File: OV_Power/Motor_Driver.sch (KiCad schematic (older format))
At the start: 20 parts, among them CN1 CONN_HEADER_R_A_2POS_2.5MM, U3 LT6106, U4 VNH5019ATR-E

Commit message: Changing connectors again, also fixed a library fubar...
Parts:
- removed CN1: CONN_HEADER_R_A_2POS_2.5MM, OpenVent:53426-0210, symbol OV_Power-rescue:CONN_HEADER_R_A_2POS_2.5MM-OpenVent
- added J8: CONN_HEADER_R_A_2POS_JST_10A, OpenVent:JST_B2PS-VHLSN, symbol OpenVent:CONN_HEADER_R_A_2POS_JST_10A
- C11, C12, C16, C17, C18, C19: symbol OV_Power-rescue:1000uF_25V_Aluminium_SMD_Capacitor,_20%-OpenVent -> OpenVent:1000uF_25V_Aluminium_SMD_Capacitor,_20%
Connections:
- net at R31.1, U4.1 (OUTA), U4.25 (OUTA)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: now also J8.2
- net at D5.2 (CATHODE), D6.1 (ANODE), U4.15 (OUTB)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: now also J8.1
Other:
- note removed: "Mates with Molex cable assembly 151370201"
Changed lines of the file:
@@
 	1    0    0    -1
 $EndComp
-Text Notes 8750 4500 0    60   ~ 0
-Mates with Molex cable assembly 151370201
 NoConn ~ 4550 3750
 Text GLabel 2050 3050 0    60   Output ~ 0
@@
 Wire Wire Line
 	8500 4500 7200 4500
-Wire Wire Line
-	8500 3950 8500 4500
 Wire Wire Line
 	6400 4150 6400 4050
@@
 	1    2600 3250
 	1    0    0    -1
-$EndComp
-$Comp
-L OV_Power-rescue:CONN_HEADER_R_A_2POS_2.5MM-OpenVent CN1
-U 1 1 5F8DD118
-P 8500 3850
-F 0 "CN1" H 8700 3650 50  0000 L BNN
-F 1 "CONN_HEADER_R_A_2POS_2.5MM" H 8500 3850 50  0001 C CNN
-F 2 "OpenVent:53426-0210" H 8500 3850 50  0001 C CNN
-F 3 "https://www.molex.com/pdm_docs/sd/534260210_sd.pdf" H 8500 3850 50  0001 C CNN
-F 4 "Molex" H 8500 3850 50  0001 C CNN "Mfr"
-F 5 "0534260210" H 8800 4150 50  0000 C CNN "Mfr_PN"
-	1    8500 3850
-	1    0    0    1
 $EndComp
 $Comp
@@
 $EndComp
 $Comp
-L OV_Power-rescue:1000uF_25V_Aluminium_SMD_Capacitor,_20%-OpenVent C11
+L OpenVent:1000uF_25V_Aluminium_SMD_Capacitor,_20% C11
 U 1 1 5F8DD0EF
 P 6550 1250
+AR Path="/5F8DD0EF" Ref="C11"  Part="1"
+AR Path="/5FADD2CF/5F8DD0EF" Ref="C11"  Part="1"
 F 0 "C11" V 6650 1350 50  0000 L BNN
 F 1 "1000uF_25V_Aluminium_SMD_Capacitor,_20%" V 6800 1340 50  0001 C CNN
@@
 	6400 3350 6750 3350
 $Comp
-L OV_Power-rescue:1000uF_25V_Aluminium_SMD_Capacitor,_20%-OpenVent C12
+L OpenVent:1000uF_25V_Aluminium_SMD_Capacitor,_20% C12
 U 1 1 5F9BE2A3
 P 7100 1250
+AR Path="/5F9BE2A3" Ref="C12"  Part="1"
+AR Path="/5FADD2CF/5F9BE2A3" Ref="C12"  Part="1"
 F 0 "C12" V 7159 1360 50  0000 L CNN
 F 1 "1000uF_25V_Aluminium_SMD_Capacitor,_20%" H 7100 1250 50  0001 C CNN
@@
 Wire Wire Line
 	6400 3350 6400 3550
-Wire Wire Line
-	8500 3350 8500 3850
 Wire Wire Line
 	6750 3400 6750 3350
@@
 	4200 2500 4200 3650
 $Comp
-L OV_Power-rescue:1000uF_25V_Aluminium_SMD_Capacitor,_20%-OpenVent C16
+L OpenVent:1000uF_25V_Aluminium_SMD_Capacitor,_20% C16
 U 1 1 5FE5727D
 P 7650 1250
+AR Path="/5FE5727D" Ref="C16"  Part="1"
+AR Path="/5FADD2CF/5FE5727D" Ref="C16"  Part="1"
 F 0 "C16" V 7709 1360 50  0000 L CNN
 F 1 "1000uF_25V_Aluminium_SMD_Capacitor,_20%" H 7650 1250 50  0001 C CNN
@@
 $EndComp
 $Comp
-L OV_Power-rescue:1000uF_25V_Aluminium_SMD_Capacitor,_20%-OpenVent C17
+L OpenVent:1000uF_25V_Aluminium_SMD_Capacitor,_20% C17
 U 1 1 5FE579F4
 P 8200 1250
+AR Path="/5FE579F4" Ref="C17"  Part="1"
+AR Path="/5FADD2CF/5FE579F4" Ref="C17"  Part="1"
 F 0 "C17" V 8259 1360 50  0000 L CNN
 F 1 "1000uF_25V_Aluminium_SMD_Capacitor,_20%" H 8200 1250 50  0001 C CNN
@@
 $EndComp
 $Comp
-L OV_Power-rescue:1000uF_25V_Aluminium_SMD_Capacitor,_20%-OpenVent C18
+L OpenVent:1000uF_25V_Aluminium_SMD_Capacitor,_20% C18
 U 1 1 5FE58241
 P 8750 1250
+AR Path="/5FE58241" Ref="C18"  Part="1"
+AR Path="/5FADD2CF/5FE58241" Ref="C18"  Part="1"
 F 0 "C18" V 8809 1360 50  0000 L CNN
 F 1 "1000uF_25V_Aluminium_SMD_Capacitor,_20%" H 8750 1250 50  0001 C CNN
@@
 $EndComp
 $Comp
-L OV_Power-rescue:1000uF_25V_Aluminium_SMD_Capacitor,_20%-OpenVent C19
+L OpenVent:1000uF_25V_Aluminium_SMD_Capacitor,_20% C19
 U 1 1 5FE58A16
 P 9300 1250
+AR Path="/5FE58A16" Ref="C19"  Part="1"
+AR Path="/5FADD2CF/5FE58A16" Ref="C19"  Part="1"
 F 0 "C19" V 9359 1360 50  0000 L CNN
 F 1 "1000uF_25V_Aluminium_SMD_Capacitor,_20%" H 9300 1250 50  0001 C CNN
@@
 Wire Wire Line
 	6100 2500 6100 3050
+$Comp
+L OpenVent:CONN_HEADER_R_A_2POS_JST_10A J8
+U 1 1 5FF9F011
+P 8600 3850
+F 0 "J8" H 8900 3650 50  0000 C CNN
+F 1 "CONN_HEADER_R_A_2POS_JST_10A" H 8800 4050 50  0001 C CNN
+F 2 "OpenVent:JST_B2PS-VHLSN" H 8800 4050 50  0001 C CNN
+F 3 "http://www.jst-mfg.com/product/pdf/eng/eVH.pdf" H 8800 4050 50  0001 C CNN
+F 4 "JST Sales America Inc." H 8600 3850 50  0001 C CNN "Mfr"
+F 5 "B2PS-VH(LF)(SN)" H 9100 4150 50  0000 C CNN "Mfr_PN"
+F 6 "CONN HEADER R/A 2POS 3.96MM" H 8600 3850 50  0001 C CNN "Desc"
+F 7 "Connector Header Through Hole, Right Angle 2 position 0.156\" (3.96mm)" H 8600 3850 50  0001 C CNN "Detailed"
+	1    8600 3850
+	1    0    0    1
+$EndComp
+Wire Wire Line
+	8500 3350 8500 3850
+Wire Wire Line
+	8500 3850 8600 3850
+Wire Wire Line
+	8600 3950 8500 3950
+Wire Wire Line
+	8500 3950 8500 4500
 $EndSCHEMATC

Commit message: updated notes
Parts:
- C11, C12, C16, C17, C18, C19: symbol OpenVent:1000uF_25V_Aluminium_SMD_Capacitor,_20% -> OV_Power-rescue:1000uF_25V_Aluminium_SMD_Capacitor,_20%-OpenVent
- J8: symbol OpenVent:CONN_HEADER_R_A_2POS_JST_10A -> OV_Power-rescue:CONN_HEADER_R_A_2POS_JST_10A-OpenVent
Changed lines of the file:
@@
 $EndComp
 $Comp
-L OpenVent:1000uF_25V_Aluminium_SMD_Capacitor,_20% C11
+L OV_Power-rescue:1000uF_25V_Aluminium_SMD_Capacitor,_20%-OpenVent C11
 U 1 1 5F8DD0EF
 P 6550 1250
@@
 	6400 3350 6750 3350
 $Comp
-L OpenVent:1000uF_25V_Aluminium_SMD_Capacitor,_20% C12
+L OV_Power-rescue:1000uF_25V_Aluminium_SMD_Capacitor,_20%-OpenVent C12
 U 1 1 5F9BE2A3
 P 7100 1250
@@
 	4200 2500 4200 3650
 $Comp
-L OpenVent:1000uF_25V_Aluminium_SMD_Capacitor,_20% C16
+L OV_Power-rescue:1000uF_25V_Aluminium_SMD_Capacitor,_20%-OpenVent C16
 U 1 1 5FE5727D
 P 7650 1250
@@
 $EndComp
 $Comp
-L OpenVent:1000uF_25V_Aluminium_SMD_Capacitor,_20% C17
+L OV_Power-rescue:1000uF_25V_Aluminium_SMD_Capacitor,_20%-OpenVent C17
 U 1 1 5FE579F4
 P 8200 1250
@@
 $EndComp
 $Comp
-L OpenVent:1000uF_25V_Aluminium_SMD_Capacitor,_20% C18
+L OV_Power-rescue:1000uF_25V_Aluminium_SMD_Capacitor,_20%-OpenVent C18
 U 1 1 5FE58241
 P 8750 1250
@@
 $EndComp
 $Comp
-L OpenVent:1000uF_25V_Aluminium_SMD_Capacitor,_20% C19
+L OV_Power-rescue:1000uF_25V_Aluminium_SMD_Capacitor,_20%-OpenVent C19
 U 1 1 5FE58A16
 P 9300 1250
@@
 	6100 2500 6100 3050
 $Comp
-L OpenVent:CONN_HEADER_R_A_2POS_JST_10A J8
+L OV_Power-rescue:CONN_HEADER_R_A_2POS_JST_10A-OpenVent J8
 U 1 1 5FF9F011
 P 8600 3850

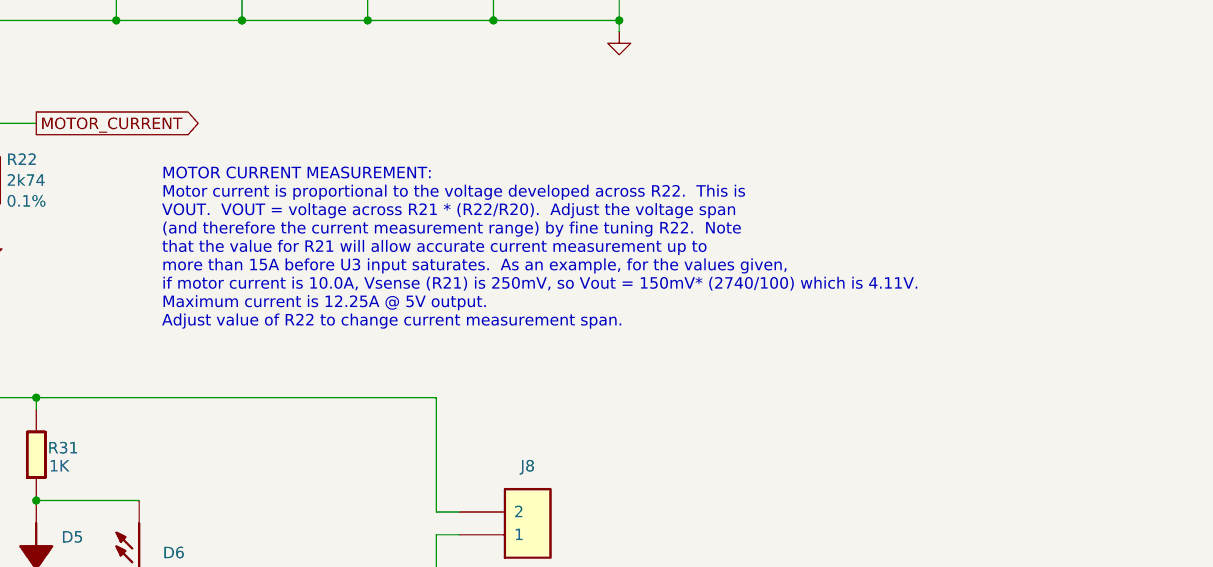
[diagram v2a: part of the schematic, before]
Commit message: Minor cleanup on power supply board.  Added Sigma Delta circuitry for A/D conversion by the FPGA, just need pin assignments for all of the signals.
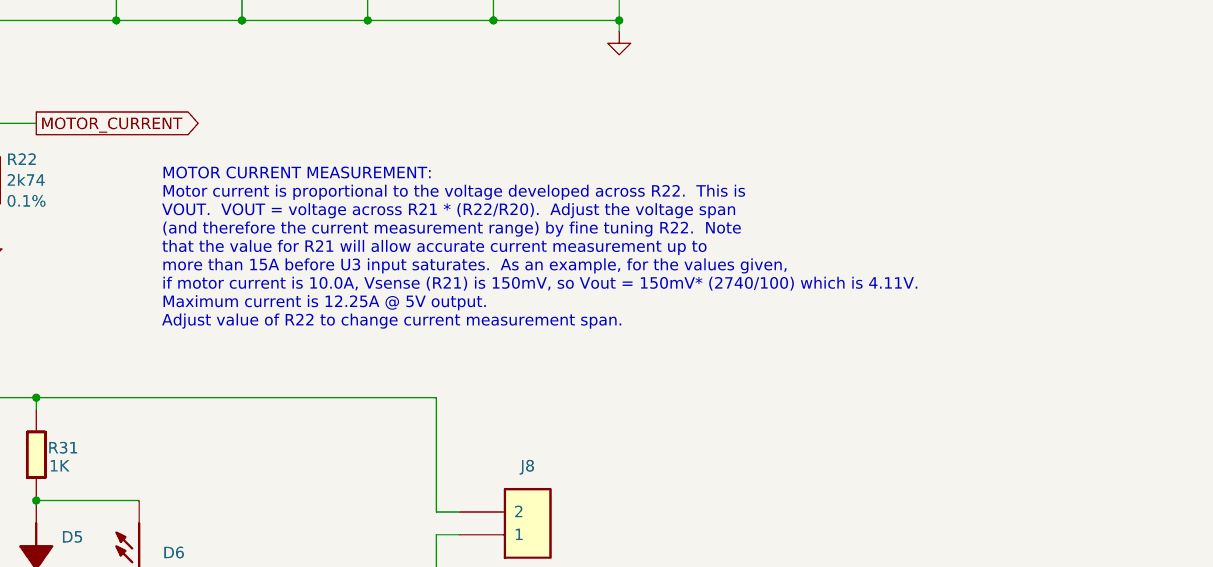
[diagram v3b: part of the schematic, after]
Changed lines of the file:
@@
 Connection ~ 6550 2150
 Text Notes 7300 3050 0    50   ~ 0
-MOTOR CURRENT MEASUREMENT:\nMotor current is proportional to the voltage developed across R22.  This is\nVOUT.  VOUT = voltage across R21 * (R22/R20).  Adjust the voltage span\n(and therefore the current measurement range) by fine tuning R22.  Note\nthat the value for R21 will allow accurate current measurement up to\nmore than 15A before U3 input saturates.  As an example, for the values given,\nif motor current is 10.0A, Vsense (R21) is 250mV, so Vout = 150mV* (2740/100) which is 4.11V.\nMaximum current is 12.25A @ 5V output.\nAdjust value of R22 to change current measurement span.
+MOTOR CURRENT MEASUREMENT:\nMotor current is proportional to the voltage developed across R22.  This is\nVOUT.  VOUT = voltage across R21 * (R22/R20).  Adjust the voltage span\n(and therefore the current measurement range) by fine tuning R22.  Note\nthat the value for R21 will allow accurate current measurement up to\nmore than 15A before U3 input saturates.  As an example, for the values given,\nif motor current is 10.0A, Vsense (R21) is 150mV, so Vout = 150mV* (2740/100) which is 4.11V.\nMaximum current is 12.25A @ 5V output.\nAdjust value of R22 to change current measurement span.
 Wire Wire Line
 	6100 1150 6550 1150

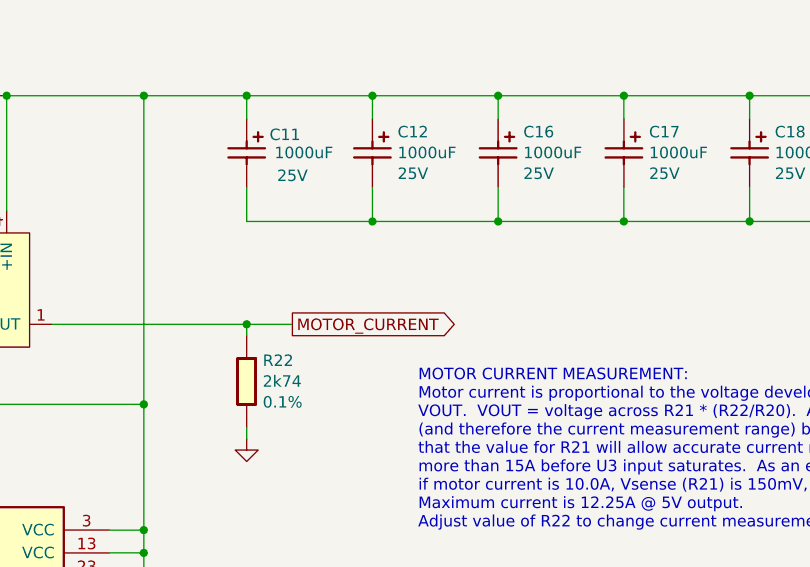
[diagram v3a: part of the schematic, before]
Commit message: Update Motor_Driver.sch
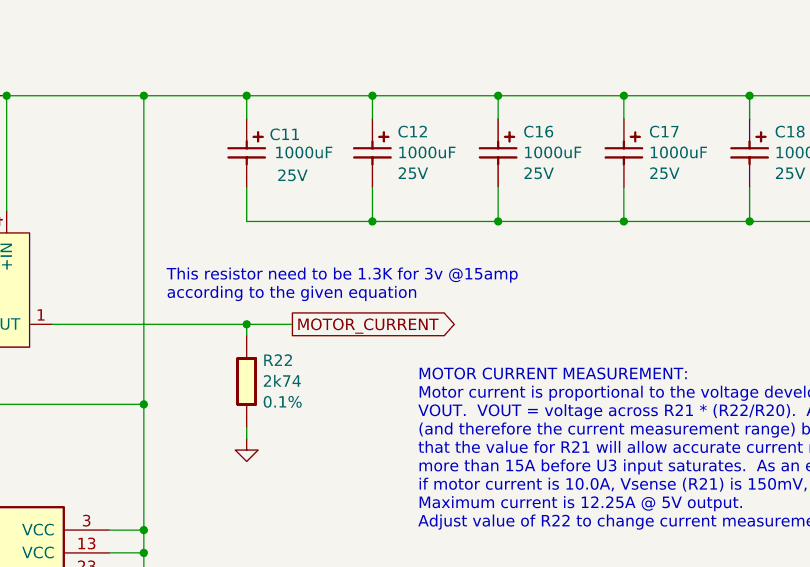
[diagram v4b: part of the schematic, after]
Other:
- note added: "This resistor need to be 1.3K for 3v @15amp\naccording to the given equation"
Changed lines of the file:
@@
 Wire Wire Line
 	8500 3950 8500 4500
+Text Notes 6200 2050 0    50   ~ 0
+This resistor need to be 1.3K for 3v @15amp\naccording to the given equation
 $EndSCHEMATC

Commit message: Update Motor_Driver.sch
R22 changed to 1.3K for 3V at 15Amp
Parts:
- removed R22: R_0603_2k74_0.1W_0.1%, Resistor_SMD:R_0603_1608Metric, symbol OV_Power-rescue:R_0603_2k74_0.1W_0.1%-OpenVent
- added R22: 1.3K-0.1%, RESC1608X55N, symbol OV_Power-rescue:1.3K-0.1%
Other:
- note removed: "This resistor need to be 1.3K for 3v @15amp\naccording to the given equation"
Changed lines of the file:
@@
 L OV_Power-rescue:GND-OpenVent #GND_014
 U 1 1 5FD604CE
-P 6550 2650
-F 0 "#GND_014" H 6550 2650 20  0001 C CNN
-F 1 "GND" H 6550 2580 50  0001 C CNN
-F 2 "" H 6550 2650 70  0000 C CNN
-F 3 "" H 6550 2650 70  0000 C CNN
-	1    6550 2650
+P 6550 2950
+F 0 "#GND_014" H 6550 2950 20  0001 C CNN
+F 1 "GND" H 6550 2880 50  0001 C CNN
+F 2 "" H 6550 2950 70  0000 C CNN
+F 3 "" H 6550 2950 70  0000 C CNN
+	1    6550 2950
 	1    0    0    -1
 $EndComp
@@
 	6550 2150 6550 2200
 Wire Wire Line
-	6550 2600 6550 2650
+	6550 2900 6550 2950
 Text GLabel 6750 2150 2    50   Output ~ 0
 MOTOR_CURRENT
@@
 Connection ~ 6550 2150
 Text Notes 7300 3050 0    50   ~ 0
-MOTOR CURRENT MEASUREMENT:\nMotor current is proportional to the voltage developed across R22.  This is\nVOUT.  VOUT = voltage across R21 * (R22/R20).  Adjust the voltage span\n(and therefore the current measurement range) by fine tuning R22.  Note\nthat the value for R21 will allow accurate current measurement up to\nmore than 15A before U3 input saturates.  As an example, for the values given,\nif motor current is 10.0A, Vsense (R21) is 150mV, so Vout = 150mV* (2740/100) which is 4.11V.\nMaximum current is 12.25A @ 5V output.\nAdjust value of R22 to change current measurement span.
+MOTOR CURRENT MEASUREMENT:\nMotor current is proportional to the voltage developed across R22.  This is\nVOUT.  VOUT = voltage across R21 * (R22/R20).  Adjust the voltage span\n(and therefore the current measurement range) by fine tuning R22.  Note\nthat the value for R21 will allow accurate current measurement up to\nmore than 15A before U3 input saturates.  As an example, for the values given,\nif motor current is 10.0A, Vsense (R21) is 150mV, so Vout = 150mV* (1300/100) which is 1.95V.\nAt 15Amp Vout = 3v\nMaximum current is 12.25A @ 5V output.\nAdjust value of R22 to change current measurement span.
 Wire Wire Line
 	6100 1150 6550 1150
@@
 	6550 1150 6550 1250
 Connection ~ 6100 1150
-$Comp
-L OV_Power-rescue:R_0603_2k74_0.1W_0.1%-OpenVent R22
-U 1 1 5FD3A248
-P 6650 2300
-F 0 "R22" V 6659 2270 50  0000 L CNN
-F 1 "R_0603_2k74_0.1W_0.1%" H 6650 2300 50  0001 C CNN
-F 2 "Resistor_SMD:R_0603_1608Metric" H 6650 2300 60  0001 C CNN
-F 3 "https://www.yageo.com/upload/media/product/productsearch/datasheet/rchip/PYu-RT_1-to-0.01_RoHS_L_12.pdf" H 6650 2300 60  0001 C CNN
-F 4 "2k74" V 6750 2270 50  0000 L CNN "Val"
-F 5 "0.1%" V 6841 2270 50  0000 L CNN "Tolerance"
-F 6 "0.1W" H 6650 2300 50  0001 C CNN "Watt"
-F 7 "Yageo" H 6650 2300 50  0001 C CNN "Mfr"
-F 8 "RT0603BRE072K74L" H 6650 2300 50  0001 C CNN "Mfr_PN"
-F 9 "RES SMD 2.74KOHM 0.1% 1/10W 0603" H 6650 2300 50  0001 C CNN "Desc"
-F 10 "2.74 kOhms ±0.1% 0.1W, 1/10W Chip Resistor 0603 (1608 Metric)  Thin Film" H 6650 2300 50  0001 C CNN "Detailed"
-	1    6650 2300
-	0    1    1    0
-$EndComp
 $Comp
 L OV_Power-rescue:R_2512_15m_cursense-OpenVent R21
@@
 Wire Wire Line
 	8500 3950 8500 4500
-Text Notes 6200 2050 0    50   ~ 0
-This resistor need to be 1.3K for 3v @15amp\naccording to the given equation
+$Comp
+L OV_Power-rescue:1.3K-0.1% R22
+U 1 1 6108DB1C
+P 6550 2200
+F 0 "R22" V 6854 2288 50  0000 L CNN
+F 1 "1.3K-0.1%" V 6945 2288 50  0000 L CNN
+F 2 "RESC1608X55N" H 7100 2250 50  0001 L CNN
+F 3 "http://www.farnell.com/datasheets/1786775.pdf" H 7100 2150 50  0001 L CNN
+F 4 "TE CONNECTIVITY - CPF0603B1K3E1 - RES, THIN FILM, 1K3, 0.1%, 0.063W, 0603" H 7100 2050 50  0001 L CNN "Description"
+F 5 "0.55" H 7100 1950 50  0001 L CNN "Height"
+F 6 "TE Connectivity" H 7100 1850 50  0001 L CNN "Manufacturer_Name"
+F 7 "CPF0603B1K3E1" H 7100 1750 50  0001 L CNN "Manufacturer_Part_Number"
+F 8 "279-CPF0603B1K3E1" H 7100 1650 50  0001 L CNN "Mouser Part Number"
+F 9 "https://www.mouser.com/Search/Refine.aspx?Keyword=279-CPF0603B1K3E1" H 7100 1550 50  0001 L CNN "Mouser Price/Stock"
+	1    6550 2200
+	0    1    1    0
+$EndComp
 $EndSCHEMATC
